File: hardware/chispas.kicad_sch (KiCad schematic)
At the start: 0 parts

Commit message: PCB: esquema, bloque de la Heltec con etiquetas y pines sin usar
Co-Authored-By: Claude Opus 5.5 <noreply@anthropic.com>
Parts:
- added U1: Heltec_WiFi_LoRa_32_V3, chispas:Heltec_WiFi_LoRa_32_V3, symbol heltec:Heltec_WiFi_LoRa_32_V3
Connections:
- new net +3.3V: U1.2 (3V3), U1.3 (3V3)
- new net AMP_SD: U1.11 (GPIO38)
- new net DAH: U1.16 (GPIO5)
- new net DECOD: U1.17 (GPIO6)
- new net DIT: U1.15 (GPIO4)
- new net ENC_CLK: U1.36 (GPIO19)
- new net ENC_DT: U1.32 (GPIO48)
- new net ENC_SW: U1.35 (GPIO20)
- new net GND: U1.1 (GND), U1.19 (GND)
- new net GPIO3: U1.14 (GPIO3)
- new net GPIO33: U1.30 (GPIO33)
- new net GPIO34: U1.29 (GPIO34)
- new net GPIO40: U1.9 (GPIO40)
- new net GPS_RX: U1.10 (GPIO39)
- new net GPS_TX: U1.31 (GPIO47)
- new net KEY: U1.13 (GPIO2)
- new net SCL: U1.7 (GPIO42)
- new net SDA: U1.8 (GPIO41)
- new net TONO: U1.18 (GPIO7)
- no-connect marks 0 -> 15

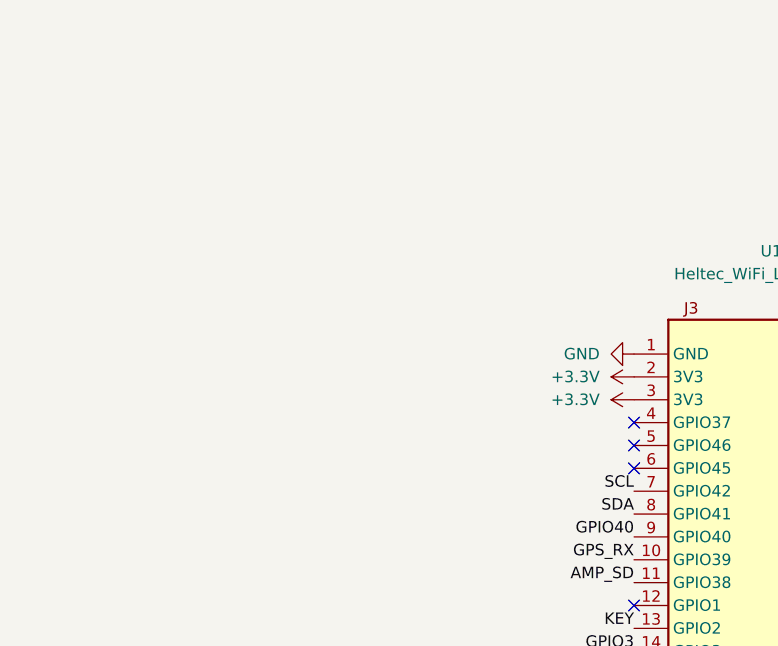
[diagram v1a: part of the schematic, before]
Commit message: PCB: bloque KEY (en curso) y tipos de pin corregidos en los simbolos importados (tipos_pines.py)
Co-Authored-By: Claude Opus 5.5 <noreply@anthropic.com>
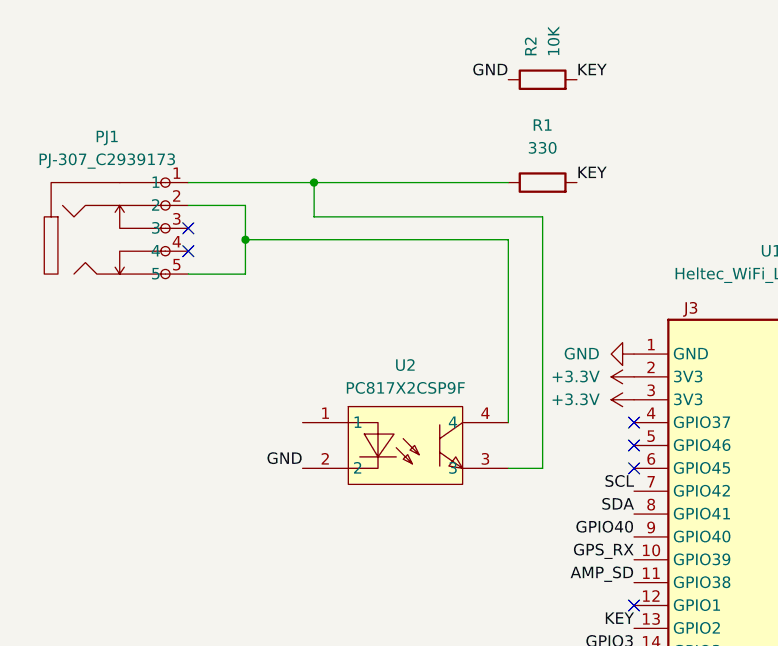
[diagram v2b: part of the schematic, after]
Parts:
- added PJ1: PJ-307_C2939173, chispas:AUDIO-TH_PJ-307, symbol chispas:PJ-307_C2939173
- added R1: 330, Resistor_SMD:R_0805_2012Metric, symbol Device:R
- added R2: 10K, Resistor_SMD:R_0805_2012Metric, symbol Device:R
- added U2: PC817X2CSP9F, chispas:SMD-4_L4.6-W6.5-P2.54-LS10.2-TL, symbol chispas:PC817X2CSP9F
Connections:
- net GND: now also R2.1, U2.2
- net KEY: now also R1.2, R2.2
- new net: PJ1.1, R1.1, U2.3
- new net: PJ1.2, PJ1.5, U2.4
- no-connect marks 15 -> 17

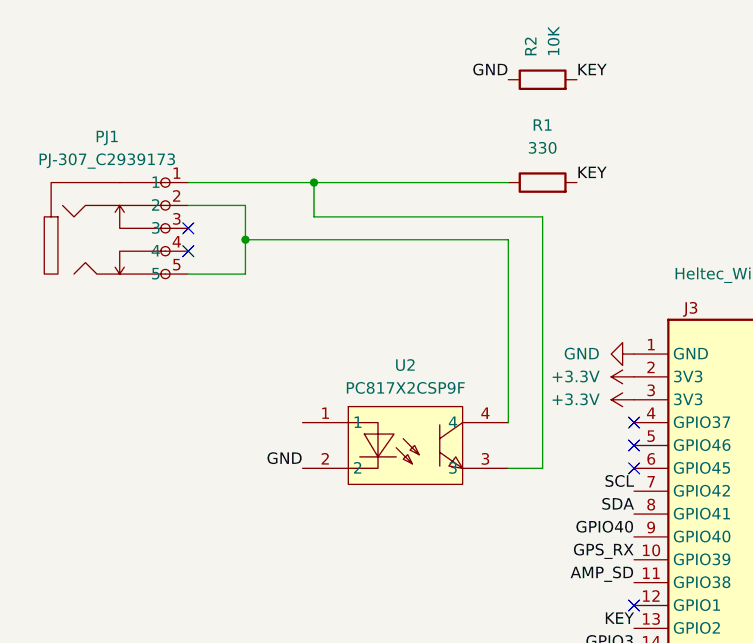
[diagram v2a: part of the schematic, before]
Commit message: PCB: bloque KEY terminado
Co-Authored-By: Claude Opus 5.5 <noreply@anthropic.com>
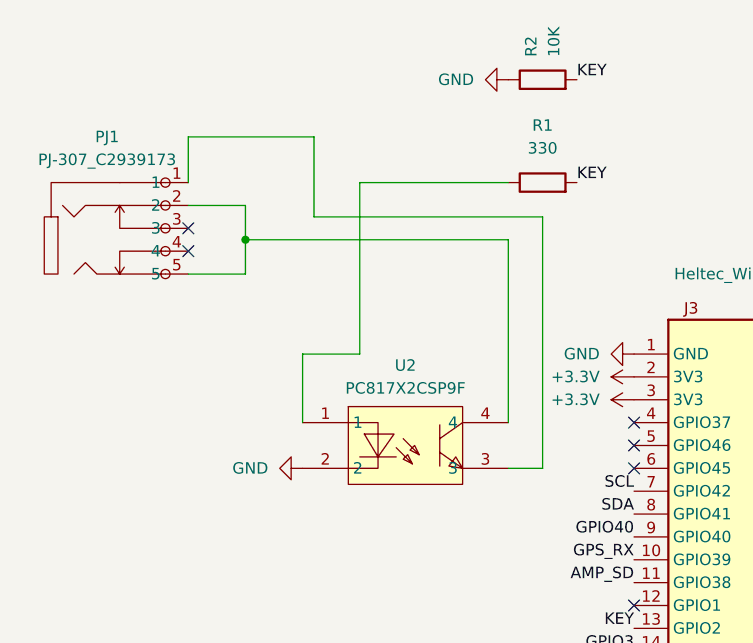
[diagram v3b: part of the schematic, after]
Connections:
- net at PJ1.1, U2.3: no longer R1.1
- net at U2.1: now also R1.1
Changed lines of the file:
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@@
 		(color 0 0 0 0)
 	)
-	(junction
-		(at 92.71 34.29)
-		(diameter 0)
-		(color 0 0 0 0)
-	)
 	(no_connect
 		(at 158.75 66.04)
@@
 	(wire
 		(pts
+			(xy 114.3 34.29) (xy 97.79 34.29)
+		)
+		(stroke
+			(width 0)
+			(type default)
+		)
+	)
+	(wire
+		(pts
+			(xy 92.71 29.21) (xy 78.74 29.21)
+		)
+		(stroke
+			(width 0)
+			(type default)
+		)
+	)
+	(wire
+		(pts
+			(xy 97.79 34.29) (xy 97.79 53.34)
+		)
+		(stroke
+			(width 0)
+			(type default)
+		)
+	)
+	(wire
+		(pts
+			(xy 91.44 53.34) (xy 91.44 60.96)
+		)
+		(stroke
+			(width 0)
+			(type default)
+		)
+	)
+	(wire
+		(pts
 			(xy 118.11 66.04) (xy 118.11 38.1)
 		)
@@
 	(wire
 		(pts
+			(xy 92.71 38.1) (xy 92.71 29.21)
+		)
+		(stroke
+			(width 0)
+			(type default)
+		)
+	)
+	(wire
+		(pts
 			(xy 114.3 60.96) (xy 114.3 40.64)
 		)
@@
 	(wire
 		(pts
-			(xy 92.71 38.1) (xy 92.71 34.29)
-		)
-		(stroke
-			(width 0)
-			(type default)
-		)
-	)
-	(wire
-		(pts
 			(xy 85.09 40.64) (xy 85.09 36.83)
 		)
@@
 	(wire
 		(pts
-			(xy 92.71 34.29) (xy 114.3 34.29)
-		)
-		(stroke
-			(width 0)
-			(type default)
-		)
-	)
-	(wire
-		(pts
-			(xy 78.74 34.29) (xy 92.71 34.29)
+			(xy 97.79 53.34) (xy 91.44 53.34)
+		)
+		(stroke
+			(width 0)
+			(type default)
+		)
+	)
+	(wire
+		(pts
+			(xy 78.74 29.21) (xy 78.74 34.29)
 		)
 		(stroke
@@
 			(width 0)
 			(type default)
-		)
-	)
-	(label "GND"
-		(at 114.3 22.86 180)
-		(effects
-			(font
-				(size 1.27 1.27)
-			)
-			(justify right bottom)
 		)
 	)
@@
 		)
 	)
-	(label "GND"
-		(at 91.44 66.04 180)
-		(effects
-			(font
-				(size 1.27 1.27)
-			)
-			(justify right bottom)
-		)
-	)
 	(label "KEY"
 		(at 121.92 22.86 0)
@@
 			)
 			(justify right bottom)
+		)
+	)
+	(symbol
+		(lib_id "power:GND")
+		(at 114.3 22.86 270)
+		(unit 1)
+		(body_style 1)
+		(exclude_from_sim no)
+		(in_bom yes)
+		(on_board yes)
+		(in_pos_files yes)
+		(dnp no)
+		(fields_autoplaced yes)
+		(property "Reference" "#PWR05"
+			(at 107.95 22.86 0)
+			(hide yes)
+			(show_name no)
+			(do_not_autoplace no)
+			(effects
+				(font
+					(size 1.27 1.27)
+				)
+			)
+		)
+		(property "Value" "GND"
+			(at 110.49 22.8599 90)
+			(show_name no)
+			(do_not_autoplace no)
+			(effects
+				(font
+					(size 1.27 1.27)
+				)
+				(justify right)
+			)
+		)
+		(property "Footprint" ""
+			(at 114.3 22.86 0)
+			(hide yes)
+			(show_name no)
+			(do_not_autoplace no)
+			(effects
+				(font
+					(size 1.27 1.27)
+				)
+			)
+		)
+		(property "Datasheet" ""
+			(at 114.3 22.86 0)
+			(hide yes)
+			(show_name no)
+			(do_not_autoplace no)
+			(effects
+				(font
+					(size 1.27 1.27)
+				)
+			)
+		)
+		(property "Description" "Power symbol creates a global label with name \"GND\" , ground"
+			(at 114.3 22.86 0)
+			(hide yes)
+			(show_name no)
+			(do_not_autoplace no)
+			(effects
+				(font
+					(size 1.27 1.27)
+				)
+			)
+		)
+		(pin "1"
+		)
+		(instances
+			(project "chispas"
+				(path "/6e07b531-5984-481f-b315-8fd49536e9dc"
+					(reference "#PWR05")
+					(unit 1)
+				)
+			)
 		)
 	)
@@
 					(unit 1)
 				)
+			)
+		)
+	)
+	(symbol
+		(lib_id "power:GND")
+		(at 91.44 66.04 270)
+		(unit 1)
+		(body_style 1)
+		(exclude_from_sim no)
+		(in_bom yes)
+		(on_board yes)
+		(in_pos_files yes)
+		(dnp no)
+		(fields_autoplaced yes)
+		(property "Reference" "#PWR06"
+			(at 85.09 66.04 0)
+			(hide yes)
+			(show_name no)
+			(do_not_autoplace no)
+			(effects
+				(font
+					(size 1.27 1.27)
+				)
+			)
+		)
+		(property "Value" "GND"
+			(at 87.63 66.0399 90)
+			(show_name no)
+			(do_not_autoplace no)
+			(effects
+				(font
+					(size 1.27 1.27)
+				)
+				(justify right)
+			)
+		)
+		(property "Footprint" ""
+			(at 91.44 66.04 0)
+			(hide yes)
+			(show_name no)
+			(do_not_autoplace no)
+			(effects
+				(font
+					(size 1.27 1.27)
+				)
+			)
+		)
+		(property "Datasheet" ""
+			(at 91.44 66.04 0)
+			(hide yes)
+			(show_name no)
+			(do_not_autoplace no)
+			(effects
+				(font
+					(size 1.27 1.27)
+				)
+			)
+		)
+		(property "Description" "Power symbol creates a global label with name \"GND\" , ground"
+			(at 91.44 66.04 0)
+			(hide yes)
+			(show_name no)
+			(do_not_autoplace no)
+			(effects
+				(font
+					(size 1.27 1.27)
+				)
+			)
+		)
+		(pin "1"
+		)
+		(instances
+			(project "chispas"
+				(path "/6e07b531-5984-481f-b315-8fd49536e9dc"
+					(reference "#PWR06")
+					(unit 1)
+				)

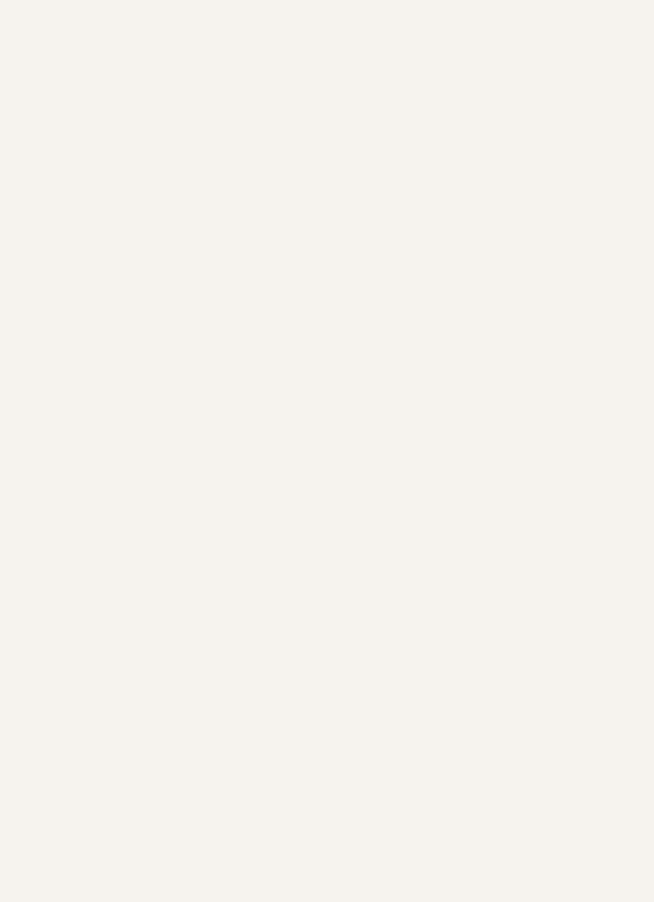
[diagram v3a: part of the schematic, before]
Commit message: PCB: palas con filtro de 10 nF, conectores JST-XH (encoder, GPS, BME280) y tira de pines libres
Co-Authored-By: Claude Opus 5.5 <noreply@anthropic.com>
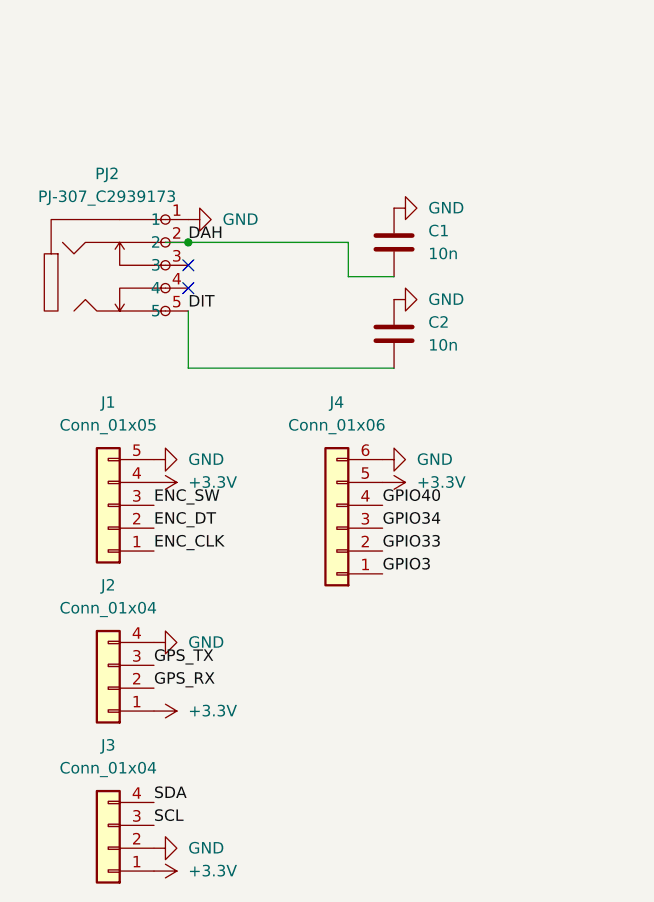
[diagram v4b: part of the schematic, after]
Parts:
- added C1, C2: 10n, Capacitor_SMD:C_0805_2012Metric, symbol Device:C
- added J1: Conn_01x05, Connector_JST:JST_XH_B5B-XH-A_1x05_P2.50mm_Vertical, symbol Connector_Generic:Conn_01x05
- added J2, J3: Conn_01x04, Connector_JST:JST_XH_B4B-XH-A_1x04_P2.50mm_Vertical, symbol Connector_Generic:Conn_01x04
- added J4: Conn_01x06, Connector_PinHeader_2.54mm:PinHeader_1x06_P2.54mm_Vertical, symbol Connector_Generic:Conn_01x06
- added PJ2: PJ-307_C2939173, chispas:AUDIO-TH_PJ-307, symbol chispas:PJ-307_C2939173
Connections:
- net +3.3V: now also J1.4 (Pin_4), J2.1 (Pin_1), J3.1 (Pin_1), J4.5 (Pin_5)
- net DAH: now also C1.2, PJ2.2
- net DIT: now also C2.2, PJ2.5
- net ENC_CLK: now also J1.1 (Pin_1)
- net ENC_DT: now also J1.2 (Pin_2)
- net ENC_SW: now also J1.3 (Pin_3)
- net GND: now also C1.1, C2.1, J1.5 (Pin_5), J2.4 (Pin_4), J3.2 (Pin_2), J4.6 (Pin_6), PJ2.1
- net GPIO3: now also J4.1 (Pin_1)
- net GPIO33: now also J4.2 (Pin_2)
- net GPIO34: now also J4.3 (Pin_3)
- net GPIO40: now also J4.4 (Pin_4)
- net GPS_RX: now also J2.2 (Pin_2)
- net GPS_TX: now also J2.3 (Pin_3)
- net SCL: now also J3.3 (Pin_3)
- net SDA: now also J3.4 (Pin_4)
- no-connect marks 17 -> 19

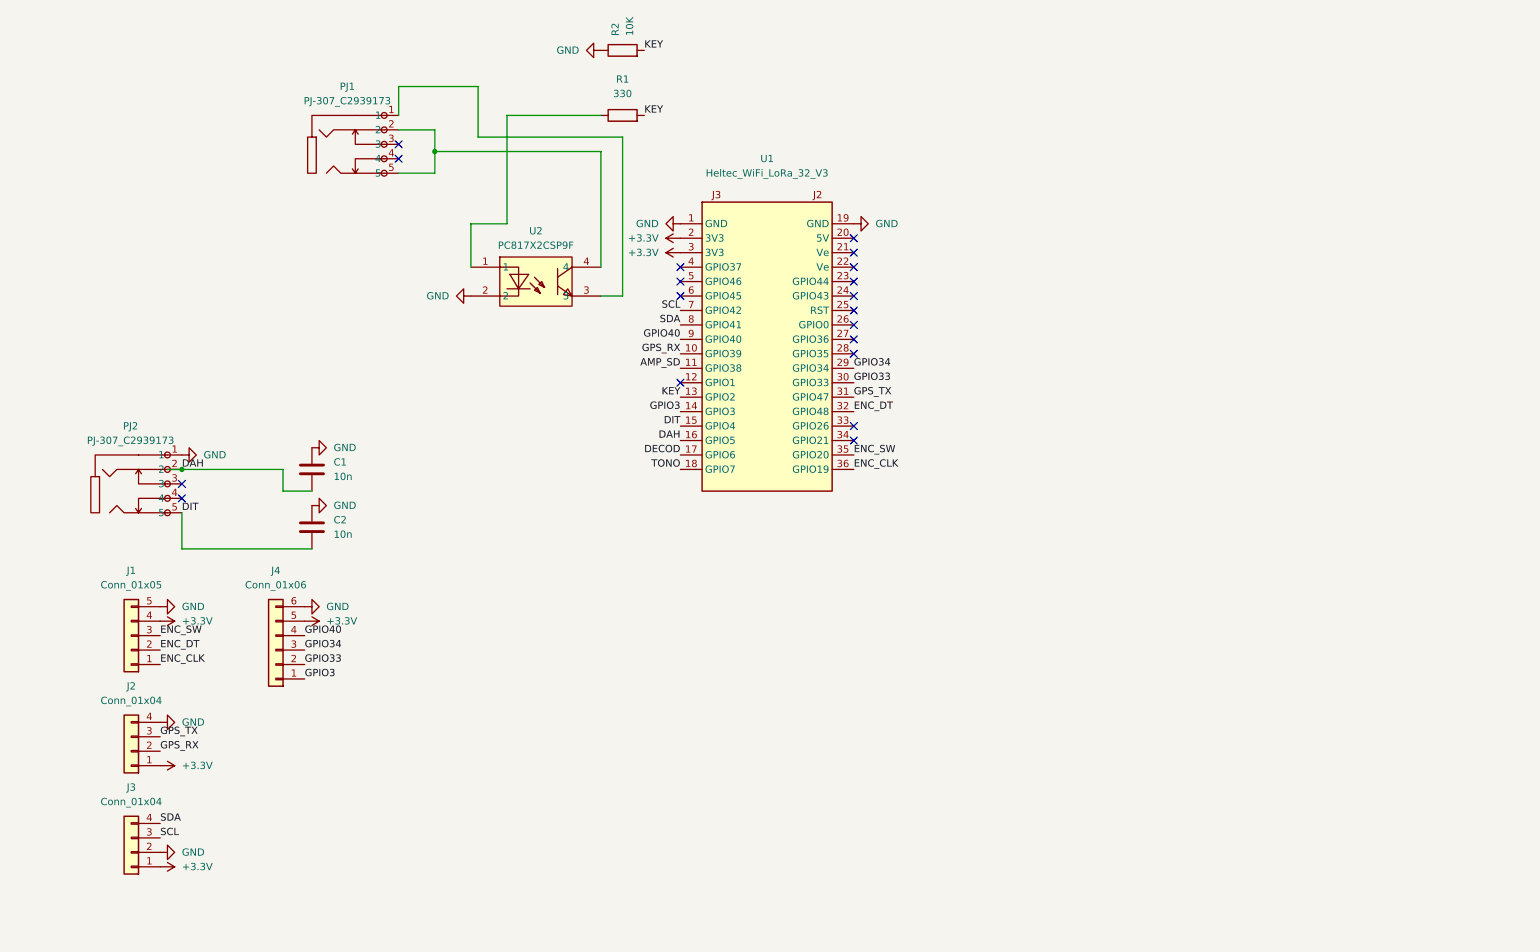
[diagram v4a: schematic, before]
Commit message: PCB: bloque de audio (volumen, auriculares y PAM8302A integrado)
Co-Authored-By: Claude Opus 5.5 <noreply@anthropic.com>
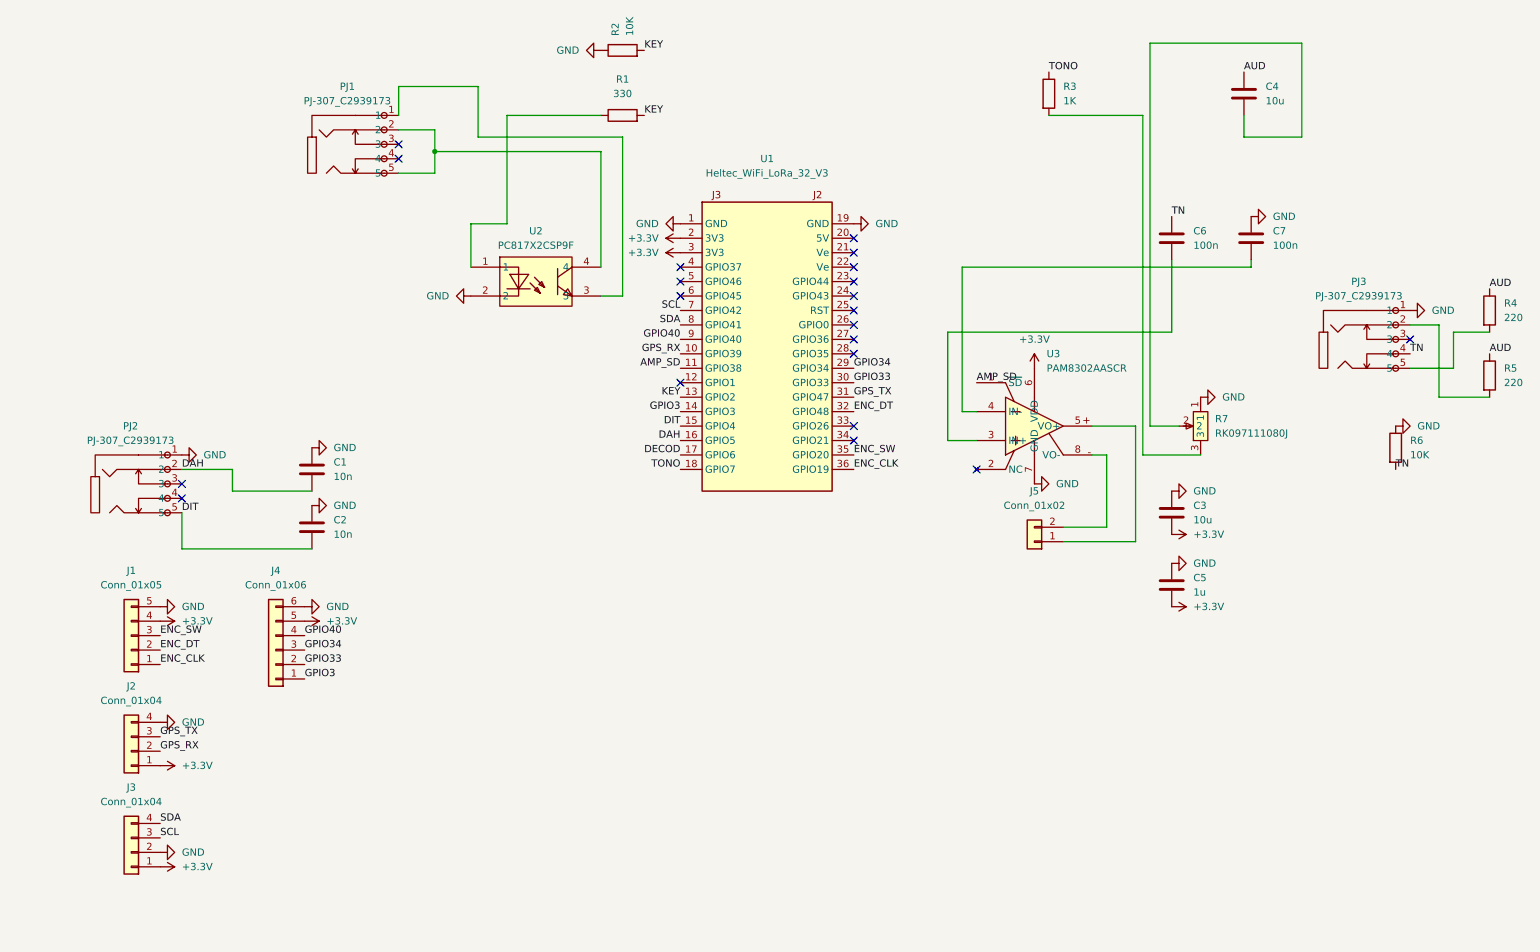
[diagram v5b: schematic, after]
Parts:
- added C3, C4: 10u, Capacitor_SMD:C_0805_2012Metric, symbol Device:C
- added C5: 1u, Capacitor_SMD:C_0805_2012Metric, symbol Device:C
- added C6, C7: 100n, Capacitor_SMD:C_0805_2012Metric, symbol Device:C
- added J5: Conn_01x02, Connector_JST:JST_PH_B2B-PH-K_1x02_P2.00mm_Vertical, symbol Connector_Generic:Conn_01x02
- added PJ3: PJ-307_C2939173, chispas:AUDIO-TH_PJ-307, symbol chispas:PJ-307_C2939173
- added R3: 1K, Resistor_SMD:R_0805_2012Metric, symbol Device:R
- added R4, R5: 220, Resistor_SMD:R_0805_2012Metric, symbol Device:R
- added R6: 10K, Resistor_SMD:R_0805_2012Metric, symbol Device:R
- added R7: RK097111080J, chispas:RES-ADJ-TH_RK097111080J, symbol chispas:RK097111080J
- added U3: PAM8302AASCR, chispas:MSOP-8_L3.0-W3.0-P0.65-LS5.0-BL, symbol chispas:PAM8302AASCR
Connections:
- net +3.3V: now also C3.2, C5.2, U3.6 (VDD)
- net AMP_SD: now also U3.1 (~{SD})
- net GND: now also C3.1, C5.1, C7.1, PJ3.1, R6.1, R7.1, U3.7 (GND)
- net TONO: now also R3.1
- new net: J5.1 (Pin_1), U3.5 (VO+)
- new net: J5.2 (Pin_2), U3.8 (VO-)
- new net: PJ3.2, R5.2
- new net: PJ3.5, R4.2
- new net: C4.2, R7.2
- new net: C6.2, U3.3 (IN+)
- new net: C7.2, U3.4 (IN-)
- new net: R3.2, R7.3
- new net AUD: C4.1, R4.1, R5.1
- new net TN: C6.1, PJ3.4, R6.2
- no-connect marks 19 -> 21
